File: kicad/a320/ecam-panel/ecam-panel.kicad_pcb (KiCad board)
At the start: 2 copper layers, 196.2 x 79.4 mm, 61 parts, among them P1 CONN_02X04, P2 CONN_01X03, P3 CONN_01X03, P4 CONN_02X05, P5 CONN_02X05, SW1 SW_PUSH_SMALL, SW10 SW_PUSH_SMALL, SW11 SW_PUSH_SMALL, SW12 SW_PUSH_SMALL, SW13 SW_PUSH_SMALL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

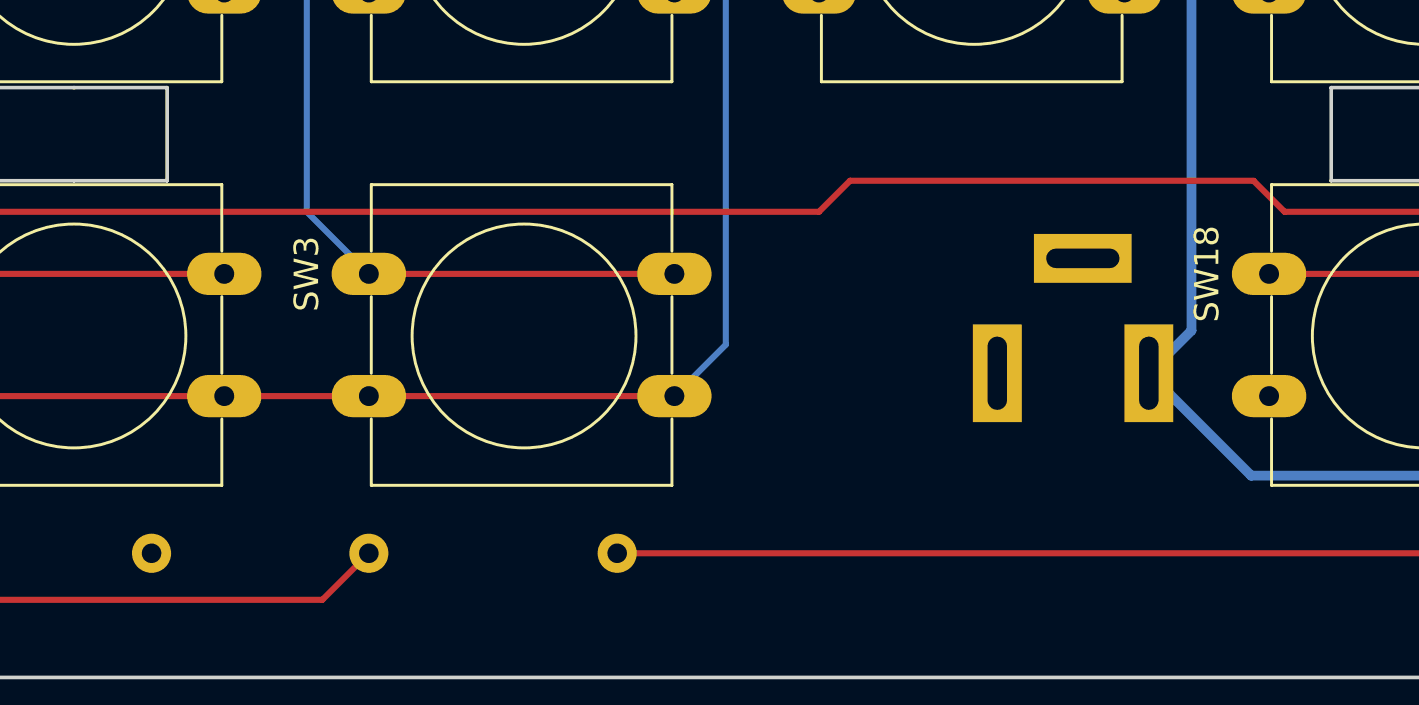
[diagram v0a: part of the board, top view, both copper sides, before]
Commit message: Fix missing tracks in A320 ECAM panel
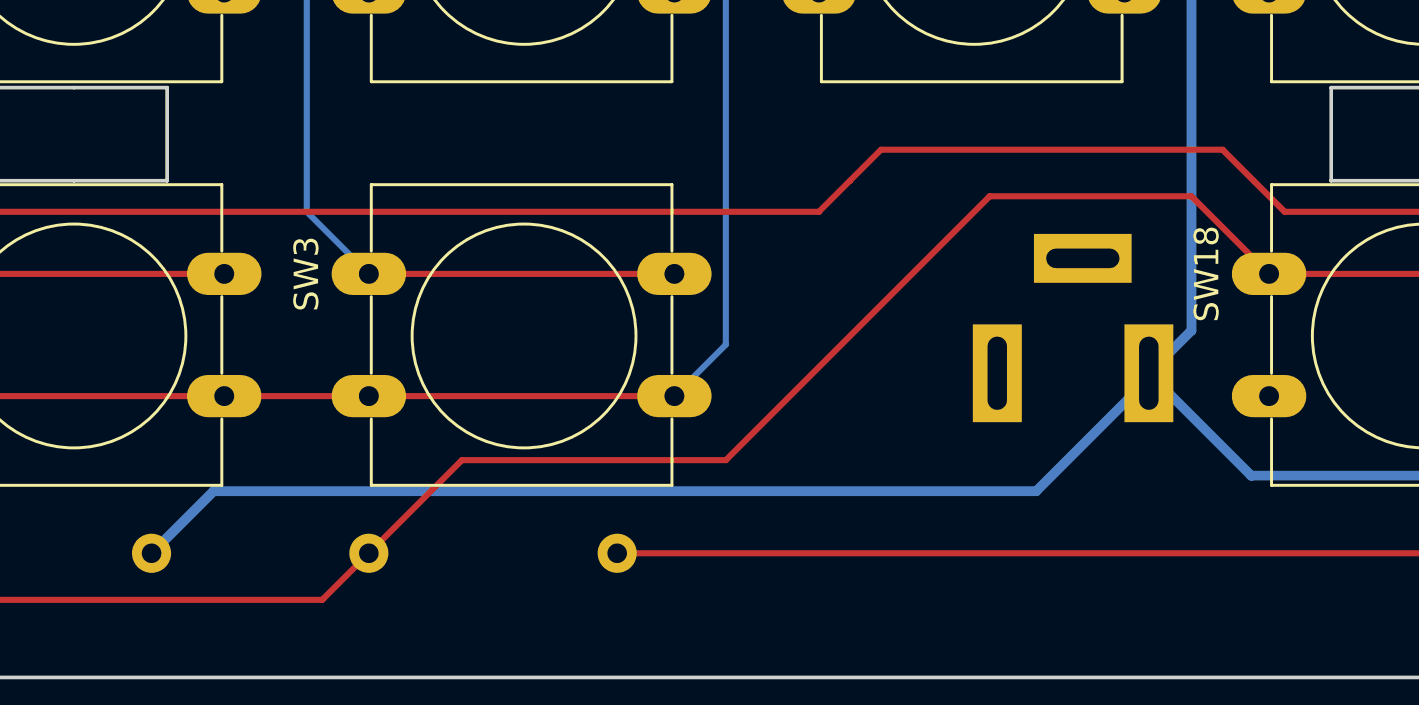
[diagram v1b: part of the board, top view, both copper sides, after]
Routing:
- net VCC: track 264.1 -> 308.3 mm
- net Net-(R2-Pad1): track 74.1 -> 118.3 mm
- net L2: track 178.5 -> 179.5 mm
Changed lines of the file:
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@@
   (general
     (links 166)
-    (no_connects 4)
+    (no_connects 2)
     (area 31.014999 37.68 228.367382 117.575001)
     (thickness 1.6)
     (drawings 108)
-    (tracks 454)
+    (tracks 466)
     (zones 0)
     (modules 61)
@@
   (gr_line (start 227.33 46.355) (end 227.33 38.1) (angle 90) (layer Margin) (width 0.2))
   (gr_line (start 226.695 38.1) (end 53.975 38.1) (angle 90) (layer Margin) (width 0.2))
+  (segment (start 133.985 112.395) (end 136.525 109.855) (width 0.4) (layer B.Cu) (net 1))
+  (segment (start 170.18 109.855) (end 174.785 105.25) (width 0.4) (layer B.Cu) (net 1))
+  (segment (start 136.525 109.855) (end 170.18 109.855) (width 0.4) (layer B.Cu) (net 1))
+  (segment (start 174.785 105.25) (end 174.785 105.03) (width 0.4) (layer B.Cu) (net 1))
+  (segment (start 174.785 105.03) (end 174.785 105.25) (width 0.4) (layer F.Cu) (net 1))
   (segment (start 212.725 50.8) (end 209.55 50.8) (width 0.4) (layer F.Cu) (net 1))
   (segment (start 220.98 80.645) (end 220.98 67.31) (width 0.4) (layer F.Cu) (net 1))
@@
   (segment (start 211.455 57.785) (end 210.82 57.15) (width 0.25) (layer B.Cu) (net 20))
   (segment (start 211.455 93.98) (end 211.455 57.785) (width 0.25) (layer B.Cu) (net 20))
+  (segment (start 162.56 97.155) (end 163.83 95.885) (width 0.25) (layer F.Cu) (net 21))
+  (segment (start 177.8 95.885) (end 179.07 97.155) (width 0.25) (layer F.Cu) (net 21))
+  (segment (start 163.83 95.885) (end 177.8 95.885) (width 0.25) (layer F.Cu) (net 21))
   (segment (start 108.585 66.675) (end 108.585 74.295) (width 0.25) (layer B.Cu) (net 21))
   (segment (start 128.905 47.625) (end 108.585 47.625) (width 0.25) (layer F.Cu) (net 21))
@@
   (segment (start 131.445 50.165) (end 128.905 47.625) (width 0.25) (layer F.Cu) (net 21))
   (segment (start 208.28 98.425) (end 208.915 99.06) (width 0.25) (layer F.Cu) (net 21))
-  (segment (start 180.34 98.425) (end 208.28 98.425) (width 0.25) (layer F.Cu) (net 21))
   (segment (start 179.07 97.155) (end 180.34 98.425) (width 0.25) (layer F.Cu) (net 21))
-  (segment (start 162.56 97.155) (end 179.07 97.155) (width 0.25) (layer F.Cu) (net 21))
+  (segment (start 180.34 98.425) (end 208.28 98.425) (width 0.25) (layer F.Cu) (net 21))
   (segment (start 161.29 98.425) (end 162.56 97.155) (width 0.25) (layer F.Cu) (net 21))
   (segment (start 108.585 98.425) (end 161.29 98.425) (width 0.25) (layer F.Cu) (net 21))
@@
   (segment (start 212.09 73.66) (end 217.805 73.66) (width 0.25) (layer F.Cu) (net 36))
   (segment (start 217.805 73.66) (end 219.075 72.39) (width 0.25) (layer F.Cu) (net 36))
+  (segment (start 142.875 112.395) (end 146.685 108.585) (width 0.25) (layer F.Cu) (net 37))
+  (segment (start 176.53 97.79) (end 179.705 100.965) (width 0.25) (layer F.Cu) (net 37))
+  (segment (start 168.275 97.79) (end 176.53 97.79) (width 0.25) (layer F.Cu) (net 37))
+  (segment (start 157.48 108.585) (end 168.275 97.79) (width 0.25) (layer F.Cu) (net 37))
+  (segment (start 146.685 108.585) (end 157.48 108.585) (width 0.25) (layer F.Cu) (net 37))
   (segment (start 123.825 112.395) (end 125.73 114.3) (width 0.25) (layer F.Cu) (net 37))
   (segment (start 140.97 114.3) (end 142.875 112.395) (width 0.25) (layer F.Cu) (net 37))

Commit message: Fix wrong width of Omron B3F pads
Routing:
- net X1: track 133.0 -> 134.0 mm
- net VCC: track 308.3 -> 309.0 mm

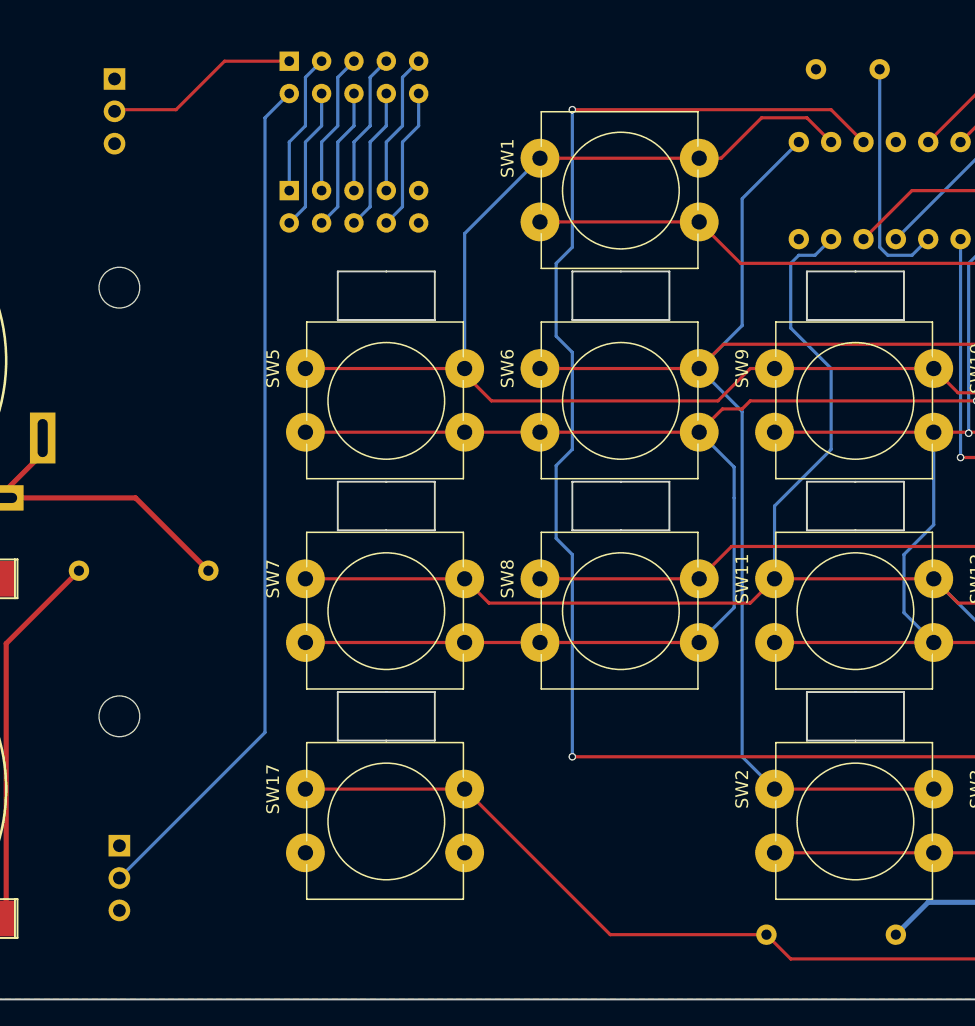
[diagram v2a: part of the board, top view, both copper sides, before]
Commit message: Fix more missing pads in A320 ECAM panel
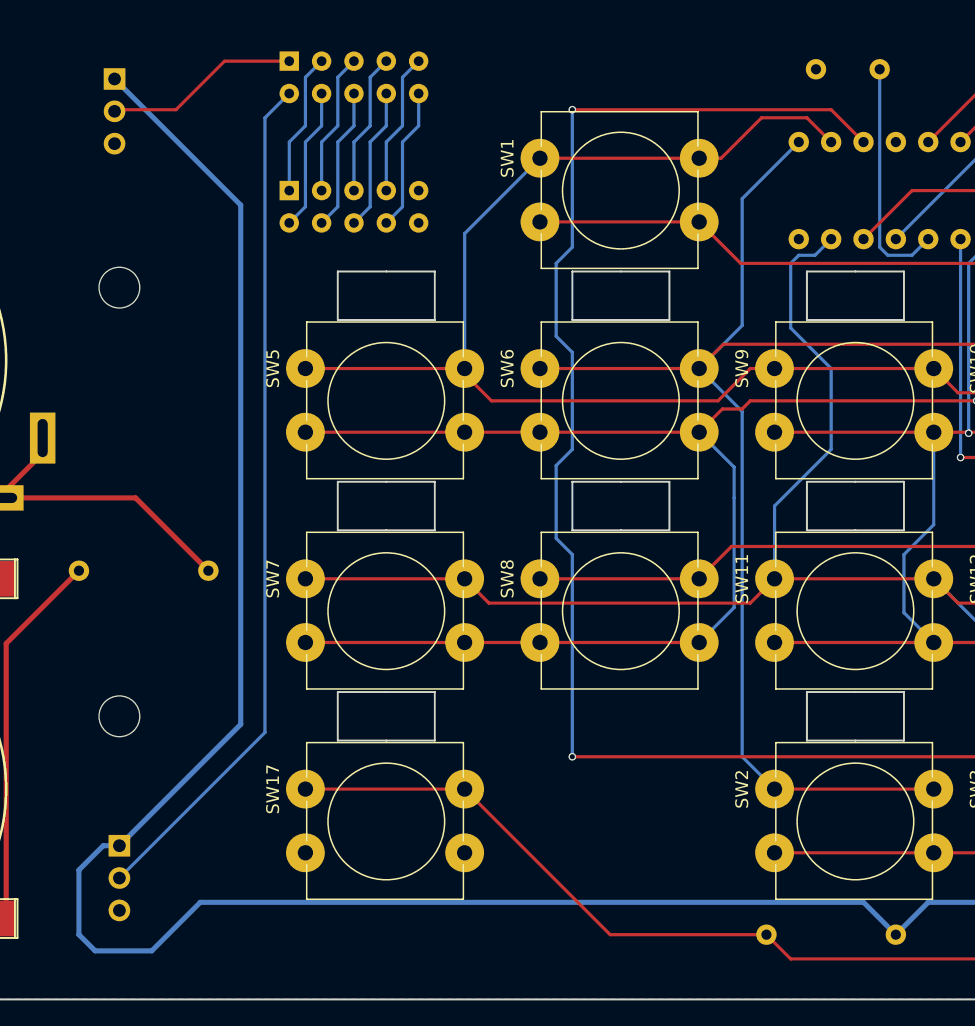
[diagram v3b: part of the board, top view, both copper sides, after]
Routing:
- net VCC: track 309.0 -> 453.5 mm
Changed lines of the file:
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@@
   (general
     (links 166)
-    (no_connects 2)
+    (no_connects 0)
     (area 31.014999 37.68 228.367382 117.575001)
     (thickness 1.6)
     (drawings 108)
-    (tracks 473)
+    (tracks 484)
     (zones 0)
     (modules 61)
@@
   (gr_line (start 227.33 46.355) (end 227.33 38.1) (angle 90) (layer Margin) (width 0.2))
   (gr_line (start 226.695 38.1) (end 53.975 38.1) (angle 90) (layer Margin) (width 0.2))
+  (segment (start 73.025 105.41) (end 82.55 95.885) (width 0.4) (layer B.Cu) (net 1))
+  (segment (start 82.55 55.118) (end 72.644 45.212) (width 0.4) (layer B.Cu) (net 1))
+  (segment (start 82.55 95.885) (end 82.55 55.118) (width 0.4) (layer B.Cu) (net 1))
+  (segment (start 133.985 112.395) (end 131.445 109.855) (width 0.4) (layer B.Cu) (net 1))
+  (segment (start 71.755 105.41) (end 73.025 105.41) (width 0.4) (layer B.Cu) (net 1))
+  (segment (start 69.85 107.315) (end 71.755 105.41) (width 0.4) (layer B.Cu) (net 1))
+  (segment (start 69.85 112.395) (end 69.85 107.315) (width 0.4) (layer B.Cu) (net 1))
+  (segment (start 71.12 113.665) (end 69.85 112.395) (width 0.4) (layer B.Cu) (net 1))
+  (segment (start 75.565 113.665) (end 71.12 113.665) (width 0.4) (layer B.Cu) (net 1))
+  (segment (start 79.375 109.855) (end 75.565 113.665) (width 0.4) (layer B.Cu) (net 1))
+  (segment (start 131.445 109.855) (end 79.375 109.855) (width 0.4) (layer B.Cu) (net 1))
   (via (at 167.64 48.895) (size 0.8) (drill 0.6) (layers F.Cu B.Cu) (net 1))
   (segment (start 167.64 48.895) (end 167.64 49.53) (width 0.4) (layer B.Cu) (net 1))

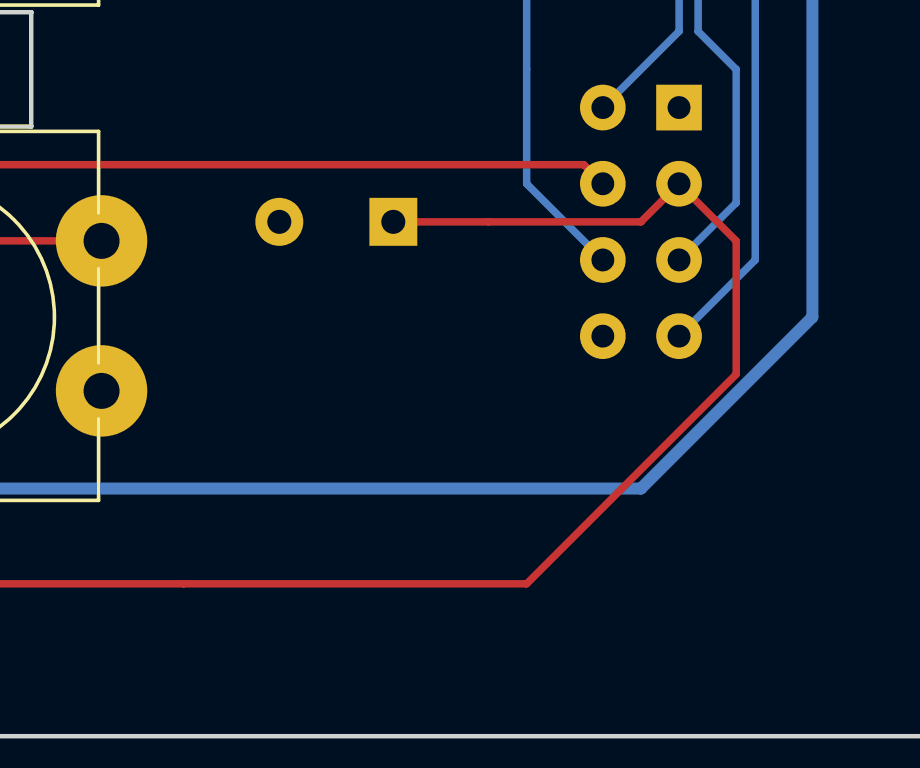
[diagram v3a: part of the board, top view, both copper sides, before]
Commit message: Minor issues and label fixings in A320 ECAM panel
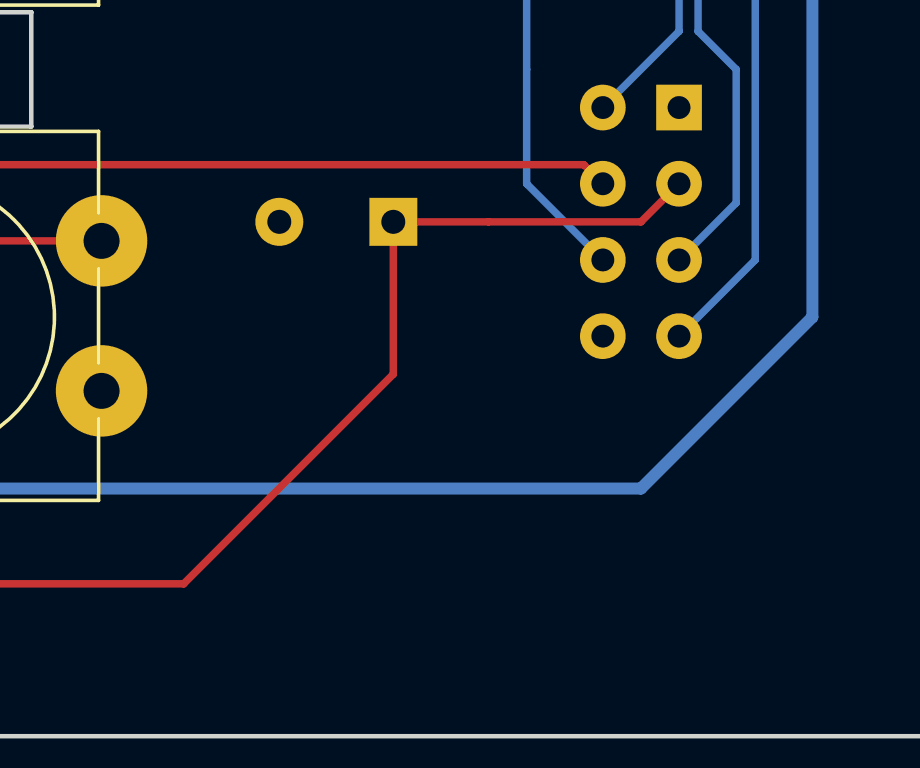
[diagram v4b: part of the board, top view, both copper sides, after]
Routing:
- net L1: track 80.4 -> 66.9 mm
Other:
- board text added: "5V PWR"
- board text added: "Avionica Project A320 ECAM Panel Rev02 Copyright (C) 2017 Alvaro Polo"
- board text added: "BL PWR"
